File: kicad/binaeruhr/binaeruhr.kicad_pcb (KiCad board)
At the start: 2 copper layers, 38 x 36 mm, 33 parts, among them U1 ATmega48PA-A, Y1 Crystal

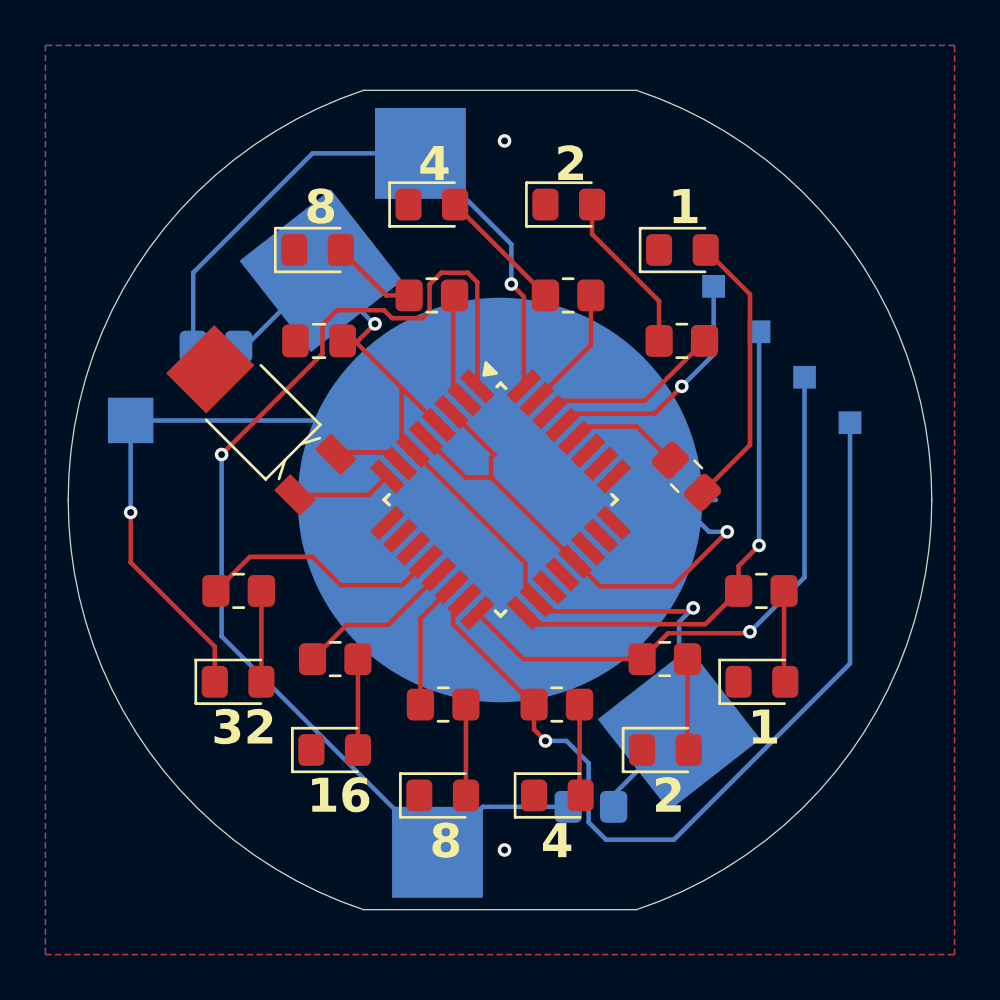
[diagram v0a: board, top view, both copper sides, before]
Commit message: use grouping to turn testing points with closer spacing. This should make Flashing easier
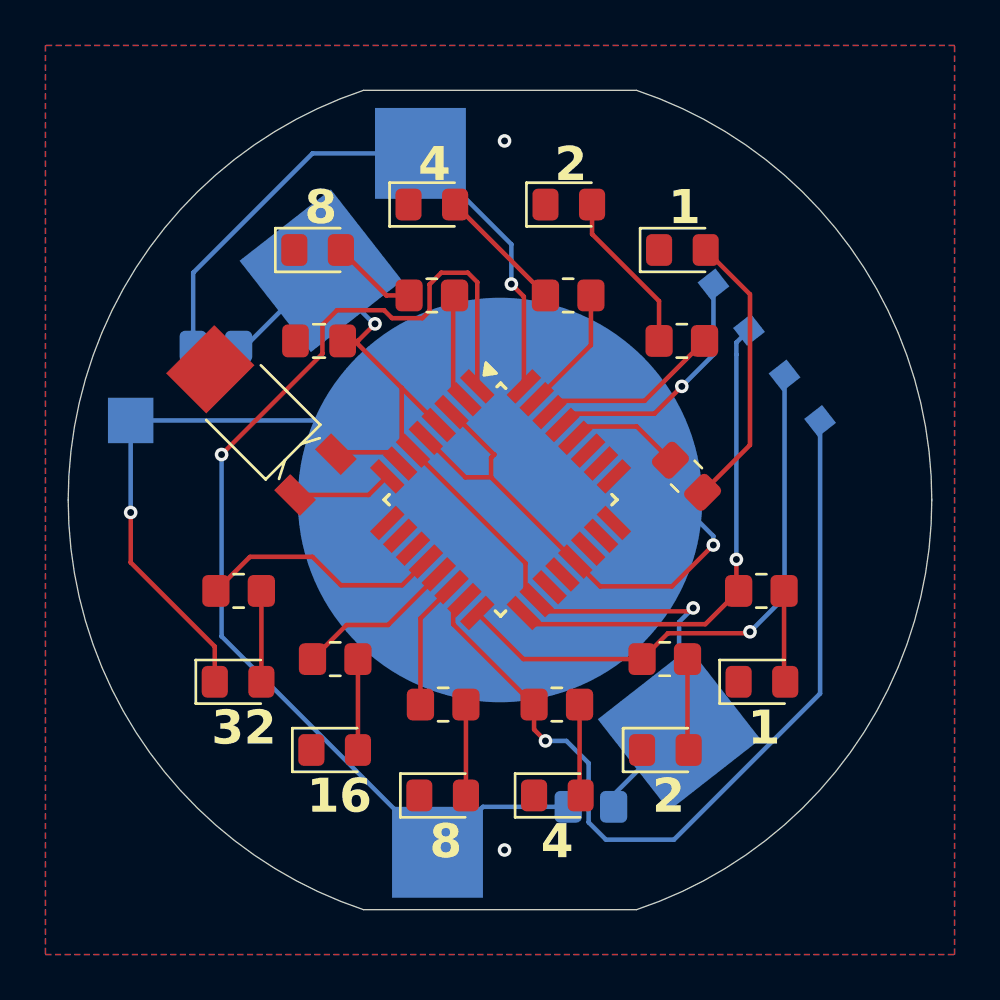
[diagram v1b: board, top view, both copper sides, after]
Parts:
- moved TP4 1.32 mm to (164.1, 96.5), turned to 128 degrees
- moved TP5 0.88 mm to (162.5, 94.5), turned to 128 degrees
- moved TP6 0.45 mm to (161.0, 92.5), turned to 128 degrees
- moved TP7 0.08 mm to (159.4, 90.5), turned to 128 degrees
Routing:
- net -BATT: track 73.1 -> 62.6 mm
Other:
- board text added: "BinäruhrV3"
- board text removed: "BinäruhrV2"
